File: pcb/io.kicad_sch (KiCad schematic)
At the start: 37 parts, among them J10 Conn_01x02, J2 RJ18, J3 RJ18, J4 Conn_02x05, J5 Conn_01x03, J6 Conn_01x03, J7 Conn_01x02, J8 Conn_01x02, J9 Conn_01x02, Q1 BT148, Q2 BC847, Q3 BC847, U7 6N137, U8 PC817, U9 PC817

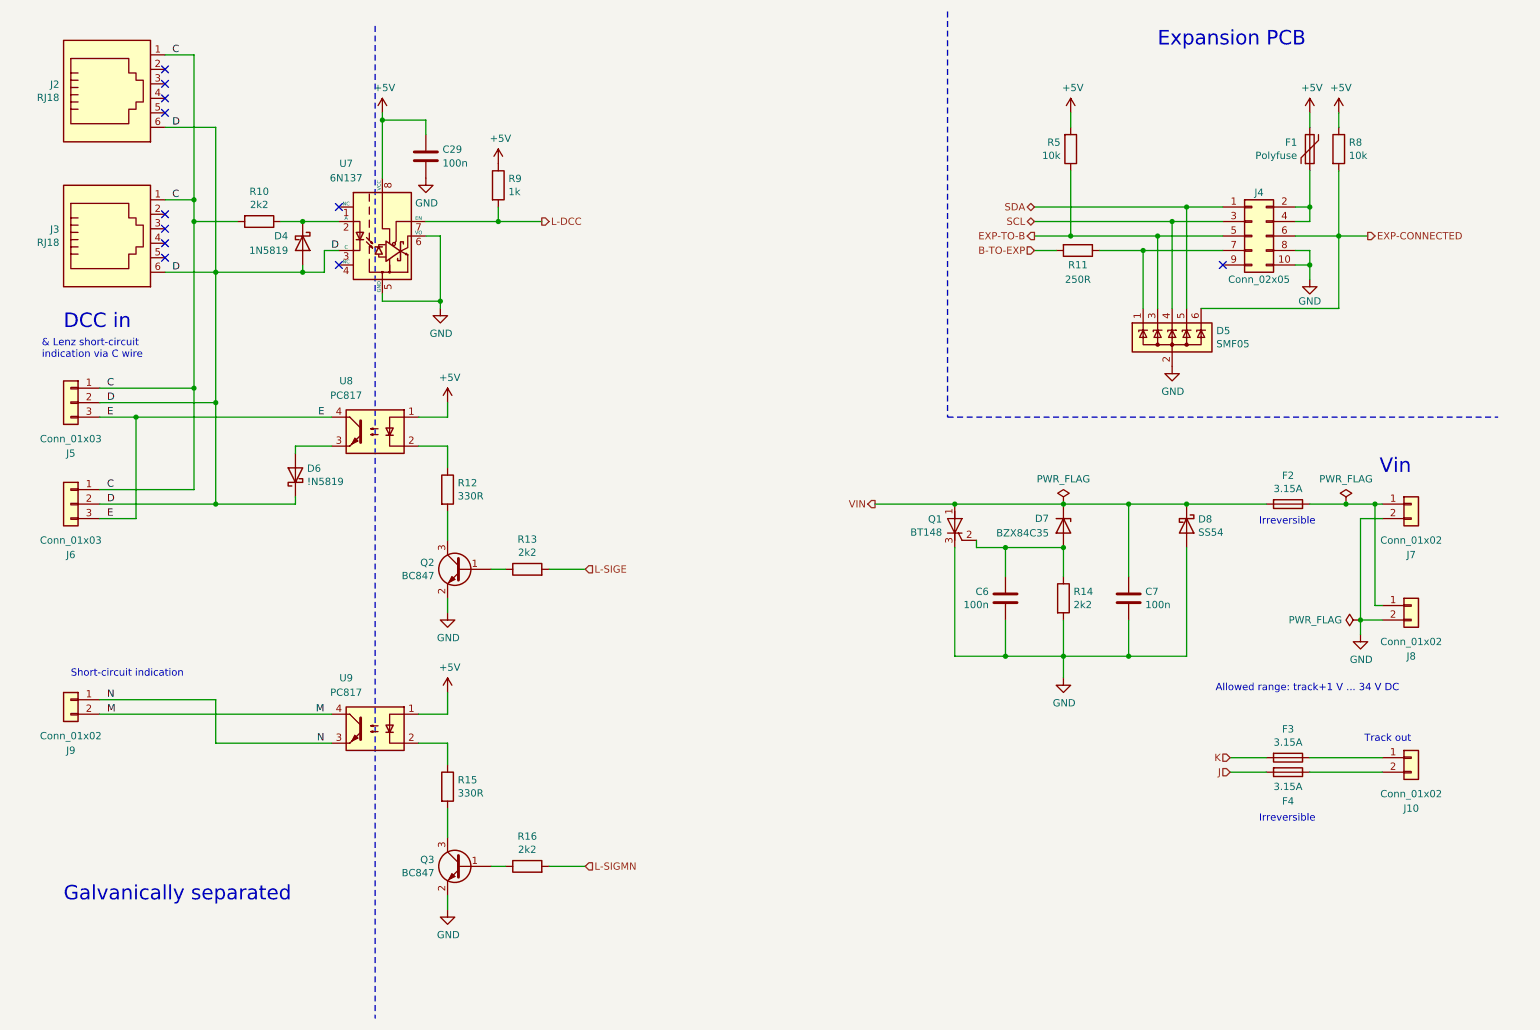
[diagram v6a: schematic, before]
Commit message: Add stabil heatsinks, minor improvements.
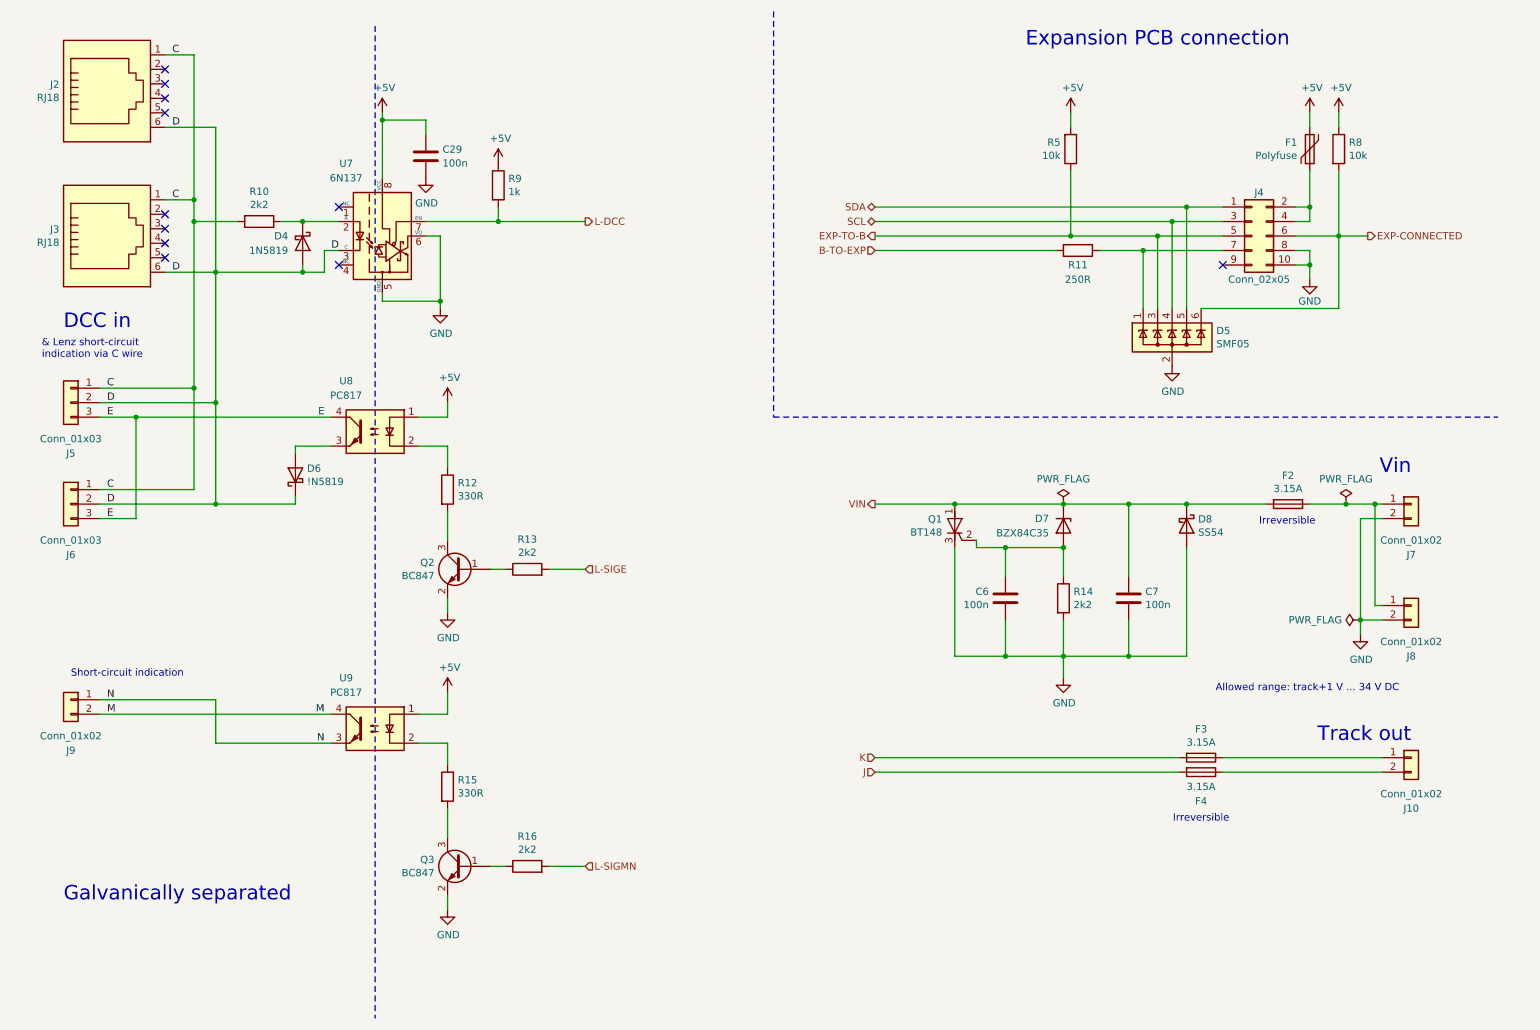
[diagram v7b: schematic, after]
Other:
- note added: "Expansion PCB connection"
- note removed: "Expansion PCB"
- moved on the sheet: F3, F4
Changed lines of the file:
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@@
 	(wire
 		(pts
-			(xy 204.47 55.88) (xy 198.12 55.88)
+			(xy 204.47 55.88) (xy 170.18 55.88)
 		)
 		(stroke
@@
 	(polyline
 		(pts
-			(xy 182.88 16.51) (xy 182.88 87.63)
+			(xy 152.4 16.51) (xy 152.4 87.63)
 		)
 		(stroke
@@
 	(polyline
 		(pts
-			(xy 182.88 87.63) (xy 279.4 87.63)
+			(xy 152.4 87.63) (xy 279.4 87.63)
 		)
 		(stroke
@@
 	(wire
 		(pts
-			(xy 198.12 53.34) (xy 222.25 53.34)
+			(xy 170.18 53.34) (xy 222.25 53.34)
 		)
 		(stroke
@@
 	(wire
 		(pts
-			(xy 104.14 53.34) (xy 111.76 53.34)
+			(xy 104.14 53.34) (xy 119.38 53.34)
 		)
 		(stroke
@@
 	(wire
 		(pts
-			(xy 246.38 147.32) (xy 259.08 147.32)
+			(xy 231.14 147.32) (xy 259.08 147.32)
 		)
 		(stroke
@@
 	(wire
 		(pts
-			(xy 238.76 147.32) (xy 232.41 147.32)
+			(xy 223.52 147.32) (xy 170.18 147.32)
 		)
 		(stroke
@@
 	(wire
 		(pts
-			(xy 246.38 149.86) (xy 259.08 149.86)
+			(xy 231.14 149.86) (xy 259.08 149.86)
 		)
 		(stroke
@@
 	(wire
 		(pts
-			(xy 201.93 58.42) (xy 198.12 58.42)
+			(xy 201.93 58.42) (xy 170.18 58.42)
 		)
 		(stroke
@@
 	(wire
 		(pts
-			(xy 232.41 149.86) (xy 238.76 149.86)
+			(xy 170.18 149.86) (xy 223.52 149.86)
 		)
 		(stroke
@@
 	(wire
 		(pts
-			(xy 198.12 50.8) (xy 224.79 50.8)
+			(xy 170.18 50.8) (xy 224.79 50.8)
 		)
 		(stroke
@@
 	(text "Irreversible"
 		(exclude_from_sim no)
-		(at 237.49 158.75 0)
+		(at 227.33 158.75 0)
 		(effects
 			(font
 				(size 1.27 1.27)
 			)
-			(justify left bottom)
+			(justify bottom)
 		)
 	)
@@
 		(effects
 			(font
-				(size 1.27 1.27)
+				(size 2.54 2.54)
 			)
 			(justify right bottom)
 		)
 	)
-	(text "Expansion PCB"
+	(text "Expansion PCB connection"
 		(exclude_from_sim no)
 		(at 219.71 22.86 0)
@@
 				(size 2.54 2.54)
 			)
-			(justify left bottom)
+			(justify bottom)
 		)
 	)
@@
 	(hierarchical_label "J"
 		(shape input)
-		(at 232.41 149.86 180)
+		(at 170.18 149.86 180)
 		(effects
 			(font
@@
 	(hierarchical_label "B-TO-EXP"
 		(shape input)
-		(at 198.12 58.42 180)
+		(at 170.18 58.42 180)
 		(effects
 			(font
@@
 	(hierarchical_label "SCL"
 		(shape bidirectional)
-		(at 198.12 53.34 180)
+		(at 170.18 53.34 180)
 		(effects
 			(font
@@
 	(hierarchical_label "EXP-TO-B"
 		(shape output)
-		(at 198.12 55.88 180)
+		(at 170.18 55.88 180)
 		(effects
 			(font
@@
 	(hierarchical_label "SDA"
 		(shape bidirectional)
-		(at 198.12 50.8 180)
+		(at 170.18 50.8 180)
 		(effects
 			(font
@@
 	(hierarchical_label "K"
 		(shape input)
-		(at 232.41 147.32 180)
+		(at 170.18 147.32 180)
 		(effects
 			(font
@@
 	(hierarchical_label "L-DCC"
 		(shape output)
-		(at 111.76 53.34 0)
+		(at 119.38 53.34 0)
 		(effects
 			(font
@@
 	(symbol
 		(lib_id "Device:Fuse")
-		(at 242.57 147.32 270)
+		(at 227.33 147.32 270)
 		(unit 1)
 		(exclude_from_sim no)
@@
 		(dnp no)
 		(property "Reference" "F3"
-			(at 242.57 142.3162 90)
+			(at 227.33 142.3162 90)
 			(effects
 				(font
@@
 		)
 		(property "Value" "3.15A"
-			(at 242.57 144.6276 90)
+			(at 227.33 144.6276 90)
 			(effects
 				(font
@@
 		)
 		(property "Footprint" "Fuse:Fuseholder_Cylinder-5x20mm_Stelvio-Kontek_PTF78_Horizontal_Open"
-			(at 242.57 145.542 90)
+			(at 227.33 145.542 90)
 			(effects
 				(font
@@
 		)
 		(property "Datasheet" "~"
-			(at 242.57 147.32 0)
+			(at 227.33 147.32 0)
 			(effects
 				(font
@@
 		)
 		(property "Description" "Fuse"
-			(at 242.57 147.32 0)
+			(at 227.33 147.32 0)
 			(effects
 				(font
@@
 	(symbol
 		(lib_id "Device:Fuse")
-		(at 242.57 149.86 270)
+		(at 227.33 149.86 270)
 		(unit 1)
 		(exclude_from_sim no)
@@
 		(dnp no)
 		(property "Reference" "F4"
-			(at 242.57 154.94 90)
+			(at 227.33 154.94 90)
 			(effects
 				(font
@@
 		)
 		(property "Value" "3.15A"
-			(at 242.57 152.4 90)
+			(at 227.33 152.4 90)
 			(effects
 				(font
@@
 		)
 		(property "Footprint" "Fuse:Fuseholder_Cylinder-5x20mm_Stelvio-Kontek_PTF78_Horizontal_Open"
-			(at 242.57 148.082 90)
+			(at 227.33 148.082 90)
 			(effects
 				(font
@@
 		)
 		(property "Datasheet" "~"
-			(at 242.57 149.86 0)
+			(at 227.33 149.86 0)
 			(effects
 				(font
@@
 		)
 		(property "Description" "Fuse"
-			(at 242.57 149.86 0)
+			(at 227.33 149.86 0)
 			(effects
 				(font

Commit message: Specify screw terminals, add footprints.
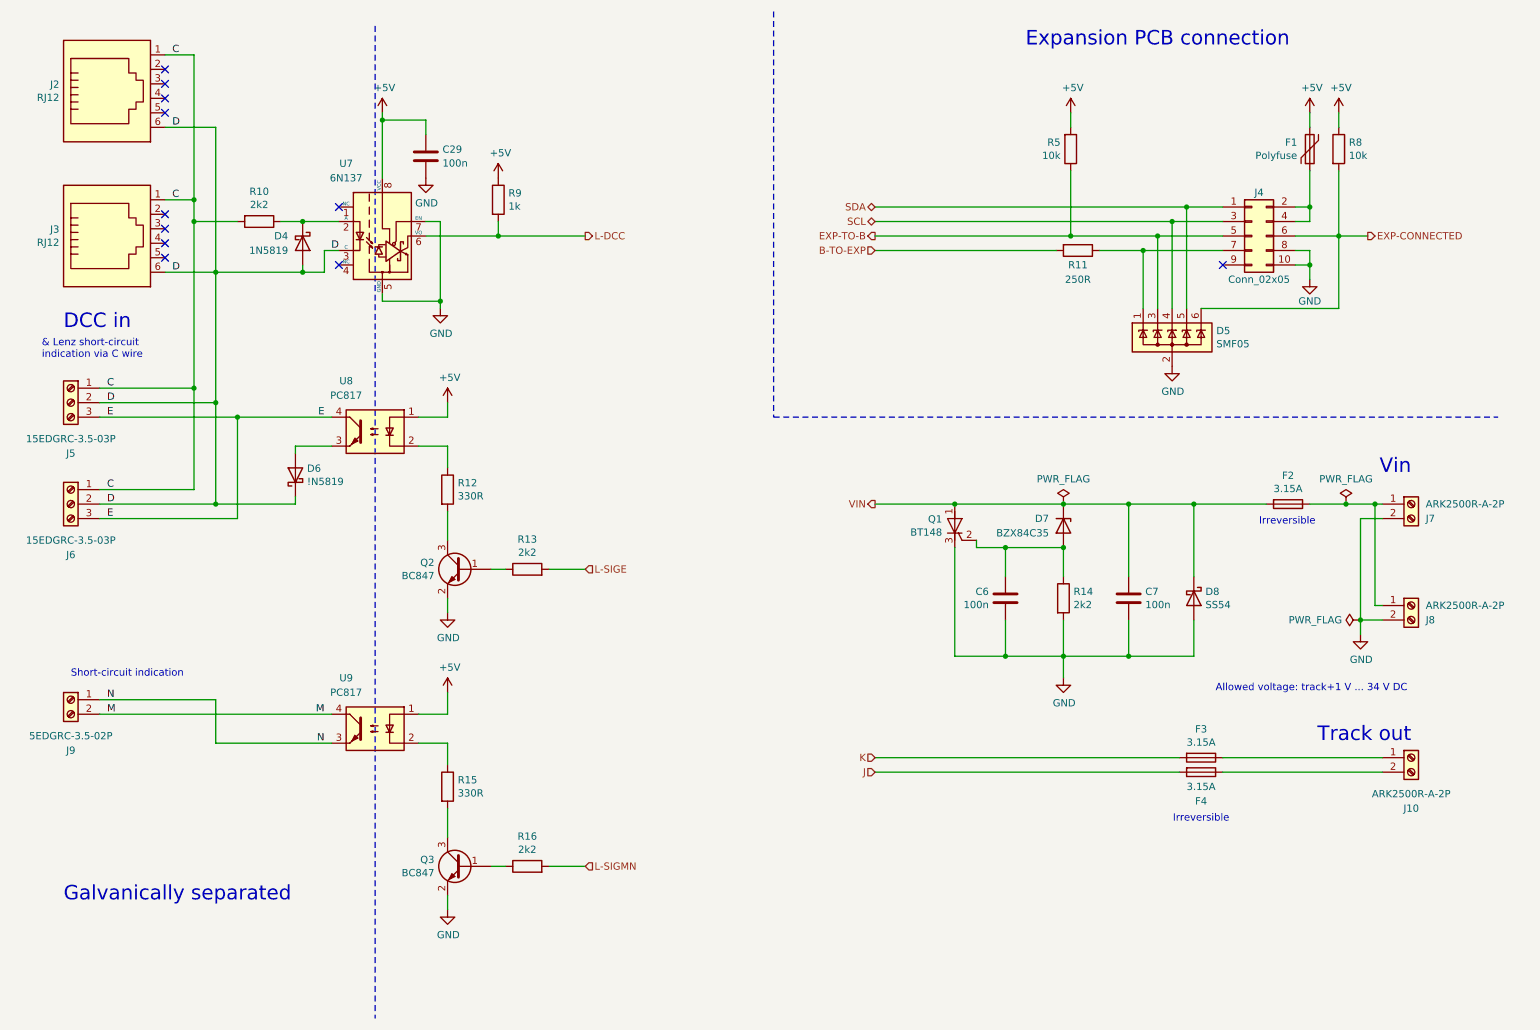
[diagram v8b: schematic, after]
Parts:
- J10, J7, J8: value Conn_01x02 -> ARK2500R-A-2P; footprint (none) -> Connector_Phoenix_MSTB:PhoenixContact_MSTBA_2,5_2-G_1x02_P5.00mm_Horizontal; symbol Connector_Generic:Conn_01x02 -> Connector:Screw_Terminal_01x02
- J2, J3: value RJ18 -> RJ12; footprint Connector_RJ:RJ12_Amphenol_54601 -> Connector_RJ:RJ25_Wayconn_MJEA-660X1_Horizontal
- J5, J6: value Conn_01x03 -> 15EDGRC-3.5-03P; footprint (none) -> Connector_Phoenix_MC:PhoenixContact_MC_1,5_3-G-3.5_1x03_P3.50mm_Horizontal; symbol Connector_Generic:Conn_01x03 -> Connector:Screw_Terminal_01x03
- J9: value Conn_01x02 -> 5EDGRC-3.5-02P; footprint (none) -> Connector_Phoenix_MC:PhoenixContact_MC_1,5_2-G-3.5_1x02_P3.50mm_Horizontal; symbol Connector_Generic:Conn_01x02 -> Connector:Screw_Terminal_01x02
- U7: footprint Package_DIP:DIP-8_W7.62mm -> Package_DIP:DIP-8_W8.89mm_SMDSocket_LongPads
- U8, U9: footprint Package_DIP:DIP-4_W7.62mm -> Package_DIP:DIP-4_W8.89mm_SMDSocket_LongPads
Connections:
- net GND: now also U7.7 (EN); no longer U7.6 (VO)
- net L-DCC: now also U7.6 (VO); no longer U7.7 (EN)
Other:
- note added: "Allowed voltage: track+1 V ... 34 V DC"
- note removed: "Allowed range: track+1 V ... 34 V DC"
- moved on the sheet: D8, R9
